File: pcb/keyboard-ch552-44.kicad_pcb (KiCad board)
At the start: 2 copper layers, 224.6 x 72.2 mm, 98 parts, among them U1 WeAct_CH552CoreBoard

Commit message: pcb: ch552-44 rev2023.1a
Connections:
- U1 pad 14: /COL6 -> unconnected-(U1-P36-Pad14)
- U1 pad 15: /COL7 -> unconnected-(U1-P37-Pad15)
- U1 pad 16: unconnected-(U1-P13-Pad16) -> /COL6
- U1 pad 17: unconnected-(U1-P12-Pad17) -> /COL7
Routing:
- net /COL7: track 190.0 -> 192.1 mm
- net /COL6: track 175.7 -> 176.6 mm

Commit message: pcb: fix SW_ value (switches are MX only)
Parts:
- SW_1_1, SW_1_2, SW_1_3, SW_1_5, SW_1_6, SW_1_7, SW_2_1, SW_2_2, SW_2_3, SW_2_4, SW_2_5, SW_2_6, SW_2_7, SW_3_1, SW_3_2, SW_3_3, SW_3_4, SW_3_5, SW_3_6, SW_3_7, SW_4_1, SW_4_2, SW_4_3, SW_4_5, SW_4_6, SW_4_7, SW_5_1, SW_5_2, SW_5_3, SW_5_5, SW_5_6, SW_5_7, SW_6_1, SW_6_2, SW_6_3, SW_6_4, SW_6_5, SW_6_6, SW_6_7, SW_7_1, SW_7_2, SW_7_4, SW_7_5, SW_7_6: value MX-compatible or Kailh Choc v1 -> MX-compatible

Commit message: pcb: CH552-44: add Comment field, adjust descriptions
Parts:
- H1, H10, H2, H3, H4, H5, H7, H8, H9: value MountingHole -> M2 mounting hole

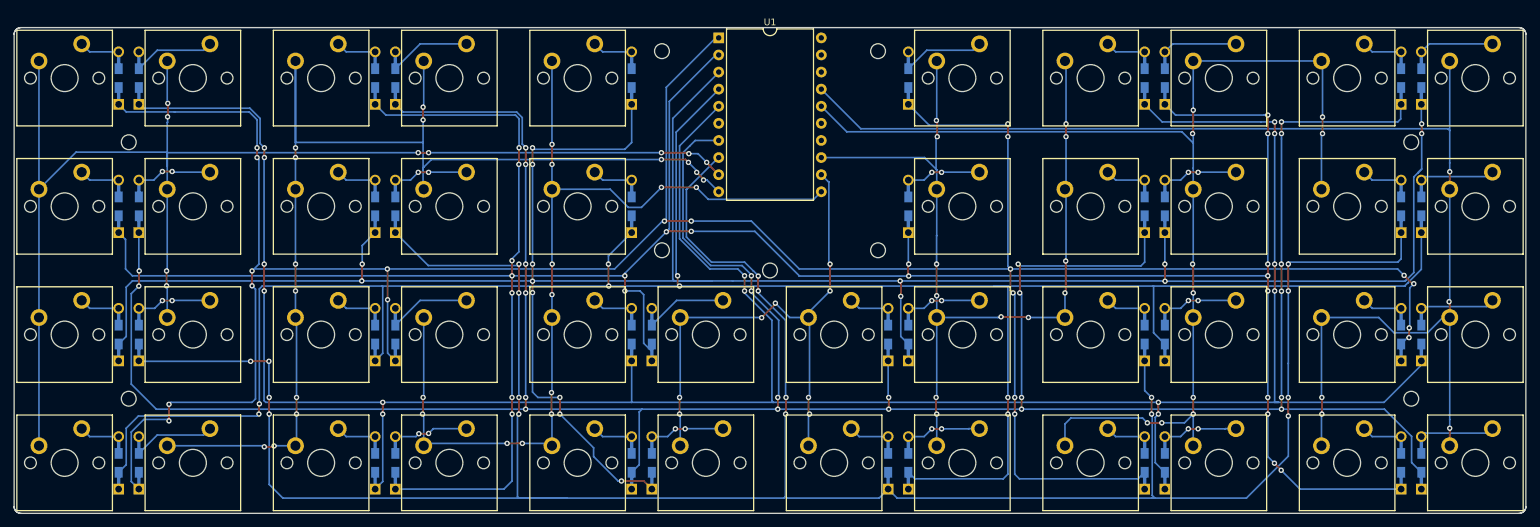
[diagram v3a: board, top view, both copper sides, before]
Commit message: pcb: update ch552-44 for rev2023.2
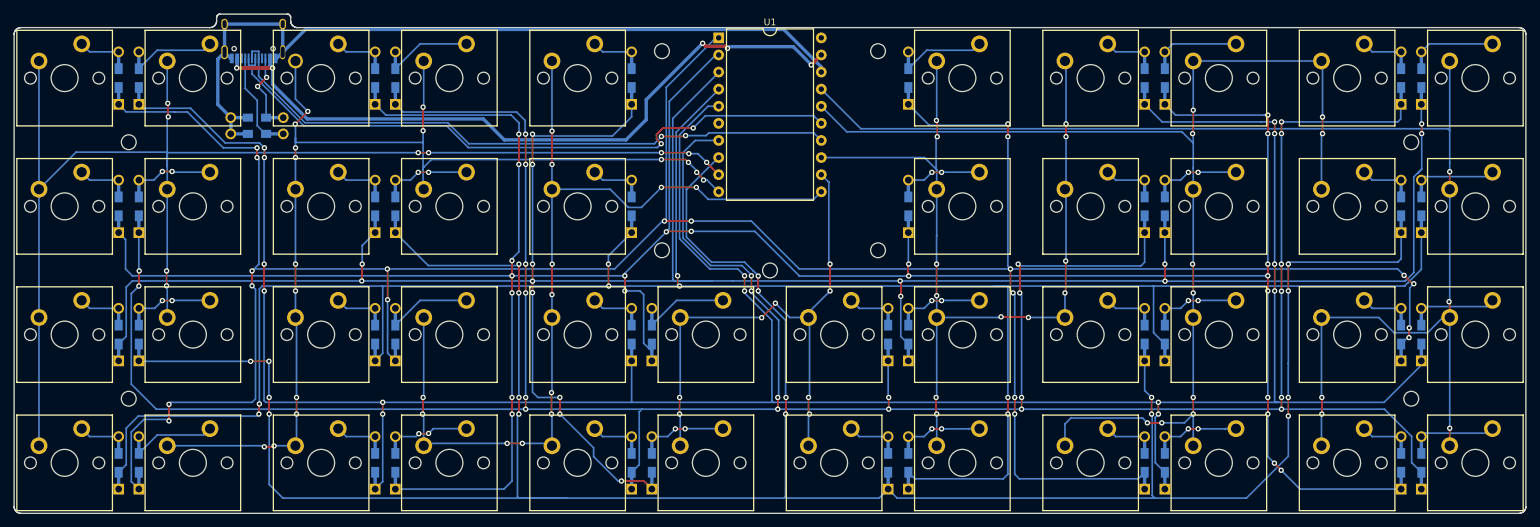
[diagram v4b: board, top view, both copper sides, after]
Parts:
- added J1: USB_C_Receptacle_USB2.0, Connector_USB:USB_C_Receptacle_HRO_TYPE-C-31-M-12, B.Cu at (85.6, 50.5)
- added R1: 5.1k, ProjectLocal:Resistor-Hybrid, B.Cu at (86.1, 63.4)
- added R2: 5.1k, ProjectLocal:Resistor-Hybrid, B.Cu at (86.1, 65.8)
- H1, H10, H2, H3, H4, H5, H7, H8, H9: value M2 mounting hole -> MountingHole
- SW_1_1, SW_1_2, SW_1_3, SW_1_5, SW_1_6, SW_1_7, SW_2_1, SW_2_2, SW_2_3, SW_2_4, SW_2_5, SW_2_6, SW_2_7, SW_3_1, SW_3_2, SW_3_3, SW_3_4, SW_3_5, SW_3_6, SW_3_7, SW_4_1, SW_4_2, SW_4_3, SW_4_5, SW_4_6, SW_4_7, SW_5_1, SW_5_2, SW_5_3, SW_5_5, SW_5_6, SW_5_7, SW_6_1, SW_6_2, SW_6_3, SW_6_4, SW_6_5, SW_6_6, SW_6_7, SW_7_1, SW_7_2, SW_7_4, SW_7_5, SW_7_6: value MX-compatible -> MX-compatible or Kailh Choc v1
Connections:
- U1 pad 14: unconnected-(U1-P36-Pad14) -> /DP
- U1 pad 15: unconnected-(U1-P37-Pad15) -> /DM
- U1 pad 18: unconnected-(U1-GND-Pad18) -> /GND
- U1 pad 19: unconnected-(U1-VBUS-Pad19) -> /VBUS
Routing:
- net /GND: track 0.00 -> 117.8 mm
- net /VBUS: track 0.00 -> 105.6 mm, vias 0 -> 5
- net /DM: track 0.00 -> 97.6 mm, vias 0 -> 2
- net /DP: track 0.00 -> 94.6 mm, vias 0 -> 2
- net Net-(J1-CC1): track 0.00 -> 12.5 mm
- net Net-(J1-CC2): track 0.00 -> 9.95 mm, vias 0 -> 2
- net /COL2: track 173.6 -> 163.7 mm, vias 14 -> 16
- net /ROW1: track 417.7 -> 415.2 mm
- net /ROW5: track 383.9 -> 382.6 mm
- net /ROW3: track 375.1 -> 374.1 mm
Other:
- board size 224.6 x 72.2 mm -> 224.6 x 74.2 mm
